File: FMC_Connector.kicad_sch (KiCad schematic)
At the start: 2 parts, among them J1 ASP-134488-01

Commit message: a little cleanup
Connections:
- net FMC_LP_CSI_C_CLK_N renamed FMC_CSI_LP_C_CLK_N
- net FMC_LP_CSI_C_CLK_P renamed FMC_CSI_LP_C_CLK_P
- net FMC_LP_CSI_C_D0_N renamed FMC_CSI_LP_C_D0_N
- net FMC_LP_CSI_C_D0_P renamed FMC_CSI_LP_C_D0_P
- net FMC_LP_CSI_C_D1_N renamed FMC_CSI_LP_C_D1_N
- net FMC_LP_CSI_C_D1_P renamed FMC_CSI_LP_C_D1_P
- net FMC_LP_CSI_D_CLK_N renamed FMC_CSI_LP_D_CLK_N
- net FMC_LP_CSI_D_CLK_P renamed FMC_CSI_LP_D_CLK_P
- net FMC_LP_CSI_D_D0_N renamed FMC_CSI_LP_D_D0_N
- net FMC_LP_CSI_D_D0_P renamed FMC_CSI_LP_D_D0_P
- net FMC_LP_CSI_D_D1_N renamed FMC_CSI_LP_D_D1_N
- net FMC_LP_CSI_D_D1_P renamed FMC_CSI_LP_D_D1_P
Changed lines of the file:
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@@
     (effects (font (size 1.27 1.27)) (justify left bottom))
   )
-  (global_label "FMC_LP_CSI_C_D1_P" (shape output) (at 118.11 73.66 0) (fields_autoplaced)
+  (global_label "FMC_CSI_LP_C_D1_P" (shape output) (at 118.11 73.66 0) (fields_autoplaced)
     (effects (font (size 1.0922 1.0922)) (justify left))
     (property "Intersheet References" "${INTERSHEET_REFS}" (id 0) (at 0 0 0)
@@
     )
   )
-  (global_label "FMC_LP_CSI_C_D0_N" (shape output) (at 118.11 83.82 0) (fields_autoplaced)
+  (global_label "FMC_CSI_LP_C_D0_N" (shape output) (at 118.11 83.82 0) (fields_autoplaced)
     (effects (font (size 1.0922 1.0922)) (justify left))
     (property "Intersheet References" "${INTERSHEET_REFS}" (id 0) (at 0 0 0)
@@
     )
   )
-  (global_label "FMC_LP_CSI_D_CLK_N" (shape output) (at 161.29 87.63 0) (fields_autoplaced)
+  (global_label "FMC_CSI_LP_D_CLK_N" (shape output) (at 161.29 87.63 0) (fields_autoplaced)
     (effects (font (size 1.0922 1.0922)) (justify left))
     (property "Intersheet References" "${INTERSHEET_REFS}" (id 0) (at 0 0 0)
@@
     )
   )
-  (global_label "FMC_LP_CSI_C_CLK_N" (shape output) (at 118.11 91.44 0) (fields_autoplaced)
+  (global_label "FMC_CSI_LP_C_CLK_N" (shape output) (at 118.11 91.44 0) (fields_autoplaced)
     (effects (font (size 1.0922 1.0922)) (justify left))
     (property "Intersheet References" "${INTERSHEET_REFS}" (id 0) (at 0 0 0)
@@
     )
   )
-  (global_label "FMC_LP_CSI_C_D1_N" (shape output) (at 118.11 76.2 0) (fields_autoplaced)
+  (global_label "FMC_CSI_LP_C_D1_N" (shape output) (at 118.11 76.2 0) (fields_autoplaced)
     (effects (font (size 1.0922 1.0922)) (justify left))
     (property "Intersheet References" "${INTERSHEET_REFS}" (id 0) (at 0 0 0)
@@
     )
   )
-  (global_label "FMC_LP_CSI_D_D1_N" (shape output) (at 161.29 72.39 0) (fields_autoplaced)
+  (global_label "FMC_CSI_LP_D_D1_N" (shape output) (at 161.29 72.39 0) (fields_autoplaced)
     (effects (font (size 1.0922 1.0922)) (justify left))
     (property "Intersheet References" "${INTERSHEET_REFS}" (id 0) (at 0 0 0)
@@
     )
   )
-  (global_label "FMC_LP_CSI_C_D0_P" (shape output) (at 118.11 81.28 0) (fields_autoplaced)
+  (global_label "FMC_CSI_LP_C_D0_P" (shape output) (at 118.11 81.28 0) (fields_autoplaced)
     (effects (font (size 1.0922 1.0922)) (justify left))
     (property "Intersheet References" "${INTERSHEET_REFS}" (id 0) (at 0 0 0)
@@
     )
   )
-  (global_label "FMC_LP_CSI_D_CLK_P" (shape output) (at 161.29 85.09 0) (fields_autoplaced)
+  (global_label "FMC_CSI_LP_D_CLK_P" (shape output) (at 161.29 85.09 0) (fields_autoplaced)
     (effects (font (size 1.0922 1.0922)) (justify left))
     (property "Intersheet References" "${INTERSHEET_REFS}" (id 0) (at 0 0 0)
@@
     )
   )
-  (global_label "FMC_LP_CSI_D_D1_P" (shape output) (at 161.29 69.85 0) (fields_autoplaced)
-    (effects (font (size 1.0922 1.0922)) (justify left))
-    (property "Intersheet References" "${INTERSHEET_REFS}" (id 0) (at 0 0 0)
-      (effects (font (size 1.27 1.27)) hide)
-    )
-  )
-  (global_label "FMC_LP_CSI_D_D0_N" (shape output) (at 161.29 80.01 0) (fields_autoplaced)
+  (global_label "FMC_CSI_LP_D_D1_P" (shape output) (at 161.29 69.85 0) (fields_autoplaced)
+    (effects (font (size 1.0922 1.0922)) (justify left))
+    (property "Intersheet References" "${INTERSHEET_REFS}" (id 0) (at 0 0 0)
+      (effects (font (size 1.27 1.27)) hide)
+    )
+  )
+  (global_label "FMC_CSI_LP_D_D0_N" (shape output) (at 161.29 80.01 0) (fields_autoplaced)
     (effects (font (size 1.0922 1.0922)) (justify left))
     (property "Intersheet References" "${INTERSHEET_REFS}" (id 0) (at 0 0 0)
@@
     )
   )
-  (global_label "FMC_LP_CSI_D_D0_P" (shape output) (at 161.29 77.47 0) (fields_autoplaced)
-    (effects (font (size 1.0922 1.0922)) (justify left))
-    (property "Intersheet References" "${INTERSHEET_REFS}" (id 0) (at 0 0 0)
-      (effects (font (size 1.27 1.27)) hide)
-    )
-  )
-  (global_label "FMC_LP_CSI_C_CLK_P" (shape output) (at 118.11 88.9 0) (fields_autoplaced)
-    (effects (font (size 1.0922 1.0922)) (justify left))
-    (property "Intersheet References" "${INTERSHEET_REFS}" (id 0) (at 0 0 0)
+  (global_label "FMC_CSI_LP_D_D0_P" (shape output) (at 161.29 77.47 0) (fields_autoplaced)
+    (effects (font (size 1.0922 1.0922)) (justify left))
+    (property "Intersheet References" "${INTERSHEET_REFS}" (id 0) (at 0 0 0)
+      (effects (font (size 1.27 1.27)) hide)
+    )
+  )
+  (global_label "FMC_CSI_LP_C_CLK_P" (shape output) (at 118.11 88.9 0) (fields_autoplaced)
+    (effects (font (size 1.0922 1.0922)) (justify left))
+    (property "Intersheet References" "${INTERSHEET_REFS}" (id 0) (at 0 0 0)

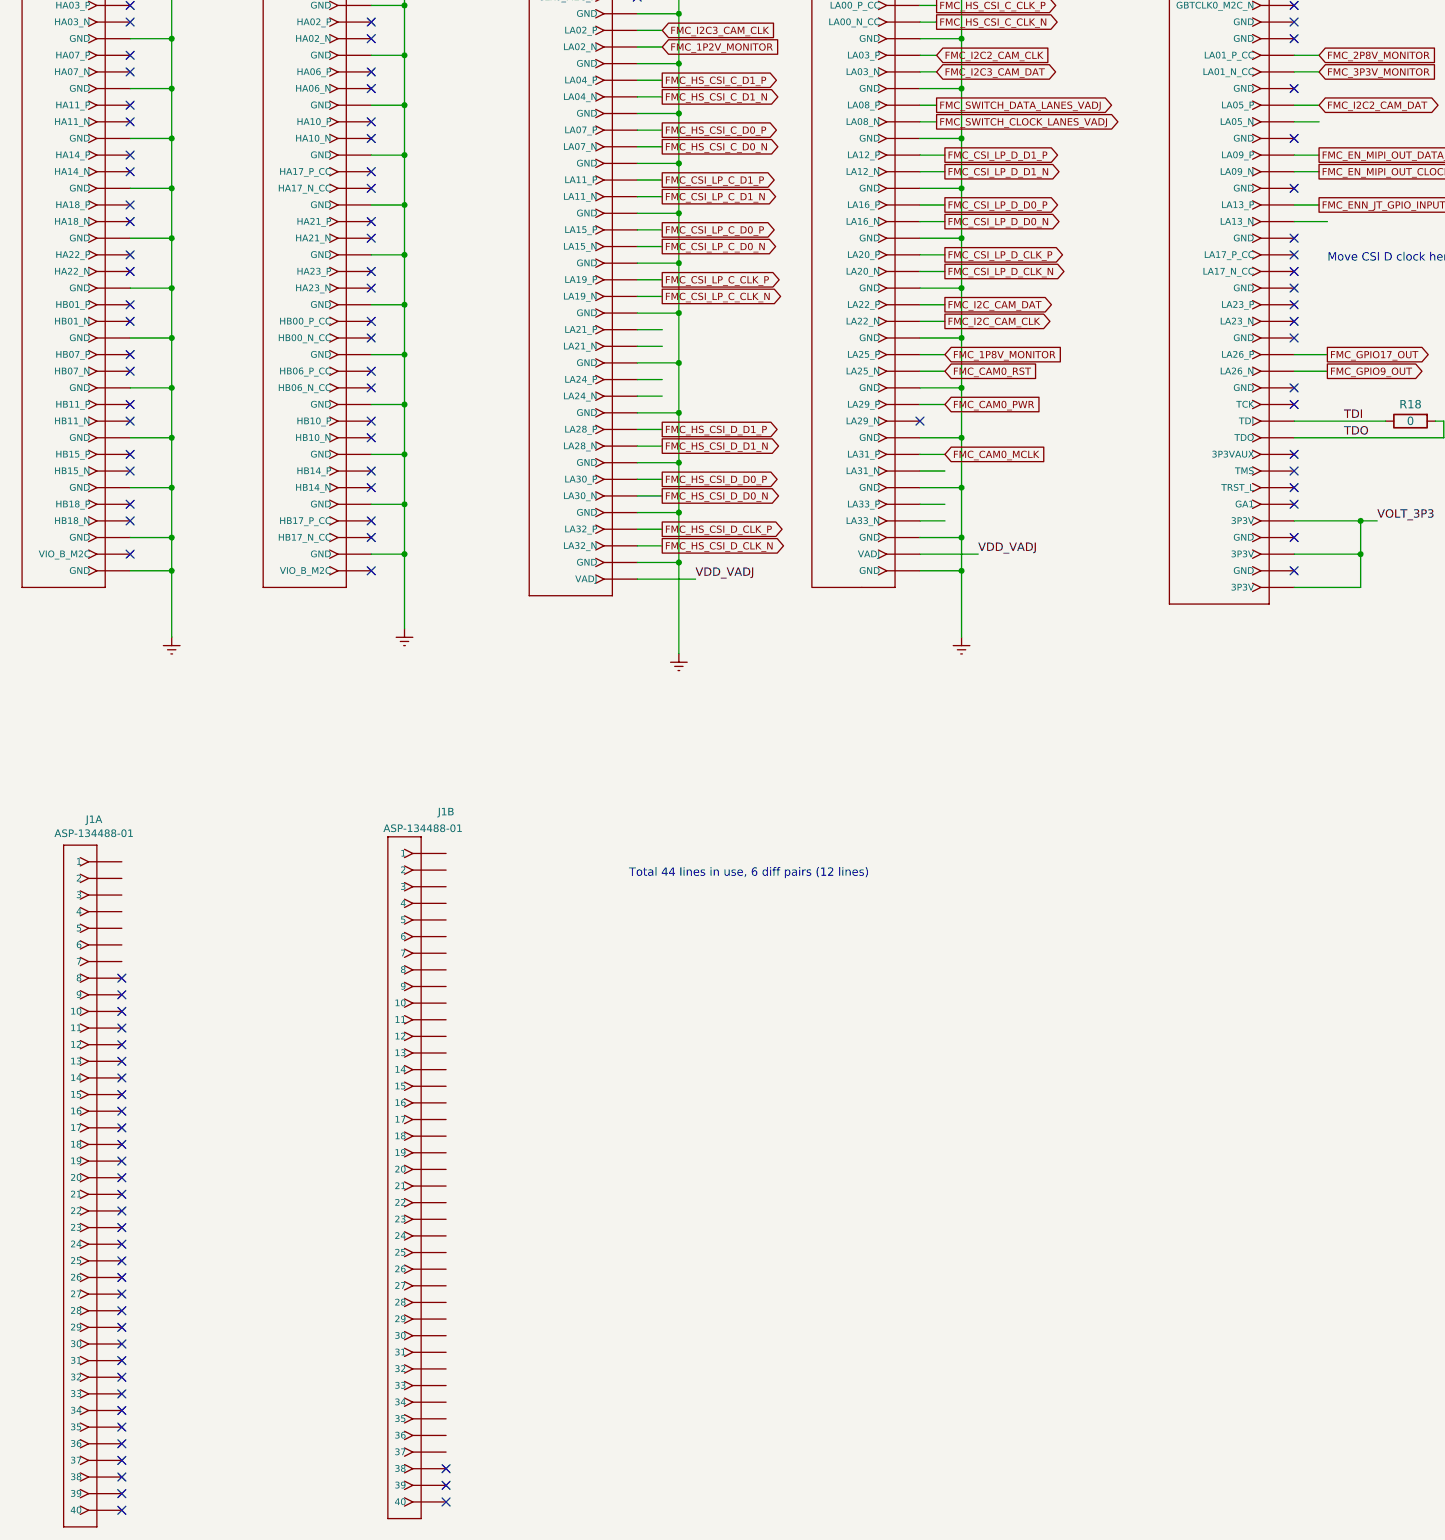
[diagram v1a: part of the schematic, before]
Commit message: DRC, ERC OK
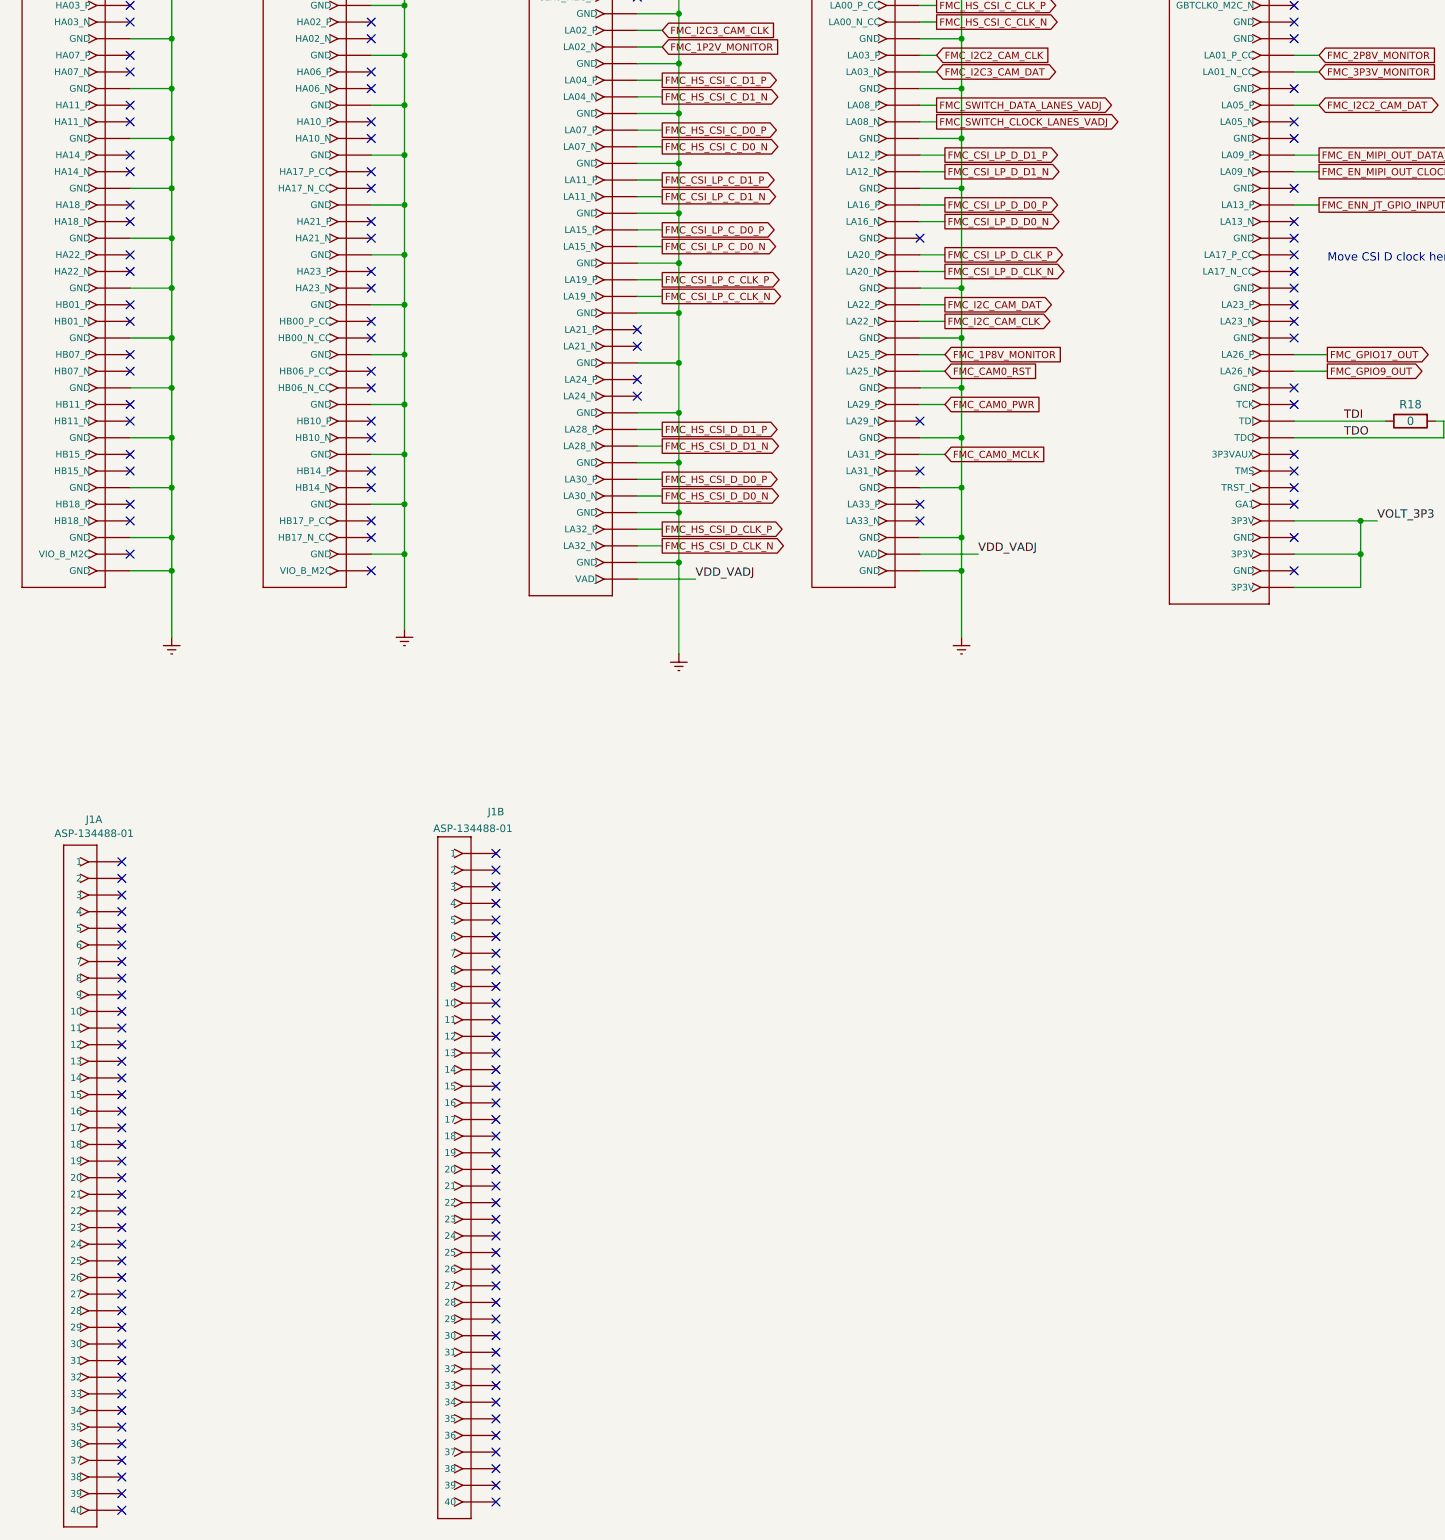
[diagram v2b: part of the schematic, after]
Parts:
- R18: symbol FMC_MIPI_v2-rescue:R-Device -> FMC_MIPI_v2:R
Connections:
- removed net Earth: J1.E1 (GND), J1.E11 (GND), J1.E14 (GND), J1.E17 (GND), J1.E20 (GND), J1.E23 (GND), J1.E26 (GND), J1.E29 (GND), J1.E32 (GND), J1.E35 (GND), J1.E38 (GND), J1.E4 (GND), J1.E40 (GND), J1.E5 (GND), J1.E8 (GND), J1.F12 (GND), J1.F15 (GND), J1.F18 (GND), J1.F2 (GND), J1.F21 (GND), J1.F24 (GND), J1.F27 (GND), J1.F3 (GND), J1.F30 (GND), J1.F33 (GND), J1.F36 (GND), J1.F39 (GND), J1.F6 (GND), J1.F9 (GND), J1.G1 (GND), J1.G11 (GND), J1.G14 (GND), J1.G17 (GND), J1.G20 (GND), J1.G23 (GND), J1.G26 (GND), J1.G29 (GND), J1.G32 (GND), J1.G35 (GND), J1.G38 (GND), J1.G4 (GND), J1.G40 (GND), J1.G5 (GND), J1.G8 (GND), J1.H12 (GND), J1.H15 (GND), J1.H18 (GND), J1.H21 (GND), J1.H24 (GND), J1.H27 (GND), J1.H3 (GND), J1.H30 (GND), J1.H33 (GND), J1.H36 (GND), J1.H39 (GND), J1.H6 (GND), J1.H9 (GND), J1.J1 (GND), J1.J11 (GND), J1.J14 (GND), J1.J17 (GND), J1.J20 (GND), J1.J23 (GND), J1.J26 (GND), J1.J29 (GND), J1.J32 (GND), J1.J35 (GND), J1.J38 (GND), J1.J4 (GND), J1.J40 (GND), J1.J5 (GND), J1.J8 (GND), J1.K12 (GND), J1.K15 (GND), J1.K18 (GND), J1.K2 (GND), J1.K21 (GND), J1.K24 (GND), J1.K27 (GND), J1.K3 (GND), J1.K30 (GND), J1.K33 (GND), J1.K36 (GND), J1.K39 (GND), J1.K6 (GND), J1.K9 (GND)
- new net: J1.E1 (GND), J1.E11 (GND), J1.E14 (GND), J1.E17 (GND), J1.E20 (GND), J1.E23 (GND), J1.E26 (GND), J1.E29 (GND), J1.E32 (GND), J1.E35 (GND), J1.E38 (GND), J1.E4 (GND), J1.E40 (GND), J1.E5 (GND), J1.E8 (GND)
- new net: J1.F12 (GND), J1.F15 (GND), J1.F18 (GND), J1.F2 (GND), J1.F21 (GND), J1.F24 (GND), J1.F27 (GND), J1.F3 (GND), J1.F30 (GND), J1.F33 (GND), J1.F36 (GND), J1.F39 (GND), J1.F6 (GND), J1.F9 (GND)
- new net: J1.G1 (GND), J1.G11 (GND), J1.G14 (GND), J1.G17 (GND), J1.G23 (GND), J1.G26 (GND), J1.G29 (GND), J1.G32 (GND), J1.G35 (GND), J1.G38 (GND), J1.G4 (GND), J1.G40 (GND), J1.G5 (GND), J1.G8 (GND)
- new net: J1.H12 (GND), J1.H15 (GND), J1.H18 (GND), J1.H21 (GND), J1.H24 (GND), J1.H27 (GND), J1.H3 (GND), J1.H30 (GND), J1.H33 (GND), J1.H36 (GND), J1.H39 (GND), J1.H6 (GND), J1.H9 (GND)
- new net: J1.J1 (GND), J1.J11 (GND), J1.J14 (GND), J1.J17 (GND), J1.J20 (GND), J1.J23 (GND), J1.J26 (GND), J1.J29 (GND), J1.J32 (GND), J1.J35 (GND), J1.J38 (GND), J1.J4 (GND), J1.J40 (GND), J1.J5 (GND), J1.J8 (GND)
- new net: J1.K12 (GND), J1.K15 (GND), J1.K18 (GND), J1.K2 (GND), J1.K21 (GND), J1.K24 (GND), J1.K27 (GND), J1.K3 (GND), J1.K30 (GND), J1.K33 (GND), J1.K36 (GND), J1.K39 (GND), J1.K6 (GND), J1.K9 (GND)
- no-connect marks 207 -> 261
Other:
- note removed: "Total 44 lines in use, 6 diff pairs (12 lines)"
- moved on the sheet: J1B

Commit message: All warnings fixed
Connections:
- net Earth: now reaches J1.E1 (GND), J1.E11 (GND), J1.E14 (GND), J1.E17 (GND), J1.E20 (GND), J1.E23 (GND), J1.E26 (GND), J1.E29 (GND), J1.E32 (GND), J1.E35 (GND), J1.E38 (GND), J1.E4 (GND), J1.E40 (GND), J1.E5 (GND), J1.E8 (GND)
- net Earth: now also J1.F12 (GND), J1.F15 (GND), J1.F18 (GND), J1.F2 (GND), J1.F21 (GND), J1.F24 (GND), J1.F27 (GND), J1.F3 (GND), J1.F30 (GND), J1.F33 (GND), J1.F36 (GND), J1.F39 (GND), J1.F6 (GND), J1.F9 (GND), J1.G1 (GND), J1.G11 (GND), J1.G14 (GND), J1.G17 (GND), J1.G23 (GND), J1.G26 (GND), J1.G29 (GND), J1.G32 (GND), J1.G35 (GND), J1.G38 (GND), J1.G4 (GND), J1.G40 (GND), J1.G5 (GND), J1.G8 (GND), J1.H12 (GND), J1.H15 (GND), J1.H18 (GND), J1.H21 (GND), J1.H24 (GND), J1.H27 (GND), J1.H3 (GND), J1.H30 (GND), J1.H33 (GND), J1.H36 (GND), J1.H39 (GND), J1.H6 (GND), J1.H9 (GND), J1.J1 (GND), J1.J11 (GND), J1.J14 (GND), J1.J17 (GND), J1.J20 (GND), J1.J23 (GND), J1.J26 (GND), J1.J29 (GND), J1.J32 (GND), J1.J35 (GND), J1.J38 (GND), J1.J4 (GND), J1.J40 (GND), J1.J5 (GND), J1.J8 (GND), J1.K12 (GND), J1.K15 (GND), J1.K18 (GND), J1.K2 (GND), J1.K21 (GND), J1.K24 (GND), J1.K27 (GND), J1.K3 (GND), J1.K30 (GND), J1.K33 (GND), J1.K36 (GND), J1.K39 (GND), J1.K6 (GND), J1.K9 (GND)

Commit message: JLCPCB BOM OK
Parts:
- J1: LCSC (none) -> NeedToAsk
- R18: LCSC (none) -> C17477; Part Number RC0805JR-070RL -> 0805W8F0000T5E
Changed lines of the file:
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@@
       (effects (font (size 1.524 1.524)) hide)
     )
+    (property "LCSC" "NeedToAsk" (id 4) (at 25.4 234.95 0)
+      (effects (font (size 1.27 1.27)) hide)
+    )
     (pin "A1")
     (pin "A10")
@@
       (effects (font (size 1.524 1.524)) hide)
     )
+    (property "LCSC" "NeedToAsk" (id 4) (at 87.63 227.33 0)
+      (effects (font (size 1.27 1.27)) hide)
+    )
     (pin "A1")
     (pin "A10")
@@
       (effects (font (size 1.524 1.524)) hide)
     )
+    (property "LCSC" "NeedToAsk" (id 4) (at 262.89 88.9 0)
+      (effects (font (size 1.27 1.27)) hide)
+    )
     (pin "A1")
     (pin "A10")
@@
       (effects (font (size 1.524 1.524)) hide)
     )
+    (property "LCSC" "NeedToAsk" (id 4) (at 209.55 87.63 0)
+      (effects (font (size 1.27 1.27)) hide)
+    )
     (pin "A1")
     (pin "A10")
@@
       (effects (font (size 1.524 1.524)) hide)
     )
+    (property "LCSC" "NeedToAsk" (id 4) (at 377.19 87.63 0)
+      (effects (font (size 1.27 1.27)) hide)
+    )
     (pin "A1")
     (pin "A10")
@@
       (effects (font (size 1.524 1.524)) hide)
     )
+    (property "LCSC" "NeedToAsk" (id 4) (at 322.58 87.63 0)
+      (effects (font (size 1.27 1.27)) hide)
+    )
     (pin "A1")
     (pin "A10")
@@
       (effects (font (size 1.524 1.524)) hide)
     )
+    (property "LCSC" "NeedToAsk" (id 4) (at 142.24 85.09 0)
+      (effects (font (size 1.27 1.27)) hide)
+    )
     (pin "A1")
     (pin "A10")
@@
       (effects (font (size 1.524 1.524)) hide)
     )
+    (property "LCSC" "NeedToAsk" (id 4) (at 96.52 87.63 0)
+      (effects (font (size 1.27 1.27)) hide)
+    )
     (pin "A1")
     (pin "A10")
@@
       (effects (font (size 1.524 1.524)) hide)
     )
+    (property "LCSC" "NeedToAsk" (id 4) (at 31.75 85.09 0)
+      (effects (font (size 1.27 1.27)) hide)
+    )
     (pin "A1")
     (pin "A10")
@@
       (effects (font (size 1.524 1.524)) hide)
     )
+    (property "LCSC" "NeedToAsk" (id 4) (at 68.58 85.09 0)
+      (effects (font (size 1.27 1.27)) hide)
+    )
     (pin "A1")
     (pin "A10")
@@
       (effects (font (size 1.27 1.27)) hide)
     )
-    (property "Datasheet" "https://www.mouser.com/ProductDetail/YAGEO/RC0805JR-070RL?qs=3ldFlDWnkKyEhdaPjQHEFA%3D%3D" (id 3) (at 232.41 110.49 0)
+    (property "Datasheet" "https://www.mouser.com/ProductDetail/Royalohm/0805W8F0000T5E?qs=e8oIoAS2J1TZ0ecBNS6tzg%3D%3D" (id 3) (at 232.41 110.49 0)
       (effects (font (size 1.27 1.27)) hide)
     )
@@
       (effects (font (size 1.524 1.524)) hide)
     )
-    (property "Part Number" "RC0805JR-070RL" (id 6) (at 232.41 110.49 90)
+    (property "Part Number" "0805W8F0000T5E" (id 6) (at 232.41 110.49 90)
       (effects (font (size 1.524 1.524)) hide)
     )
+    (property "LCSC" "C17477" (id 7) (at 388.62 198.12 90)
+      (effects (font (size 1.27 1.27)) hide)
+    )
     (pin "1")
